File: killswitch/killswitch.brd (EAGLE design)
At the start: 42.3 x 42.3 mm, 28 parts, among them U1 CD74AC20M96, U2 MMBT2222ALT1G, U3 MMBT3906LT1G

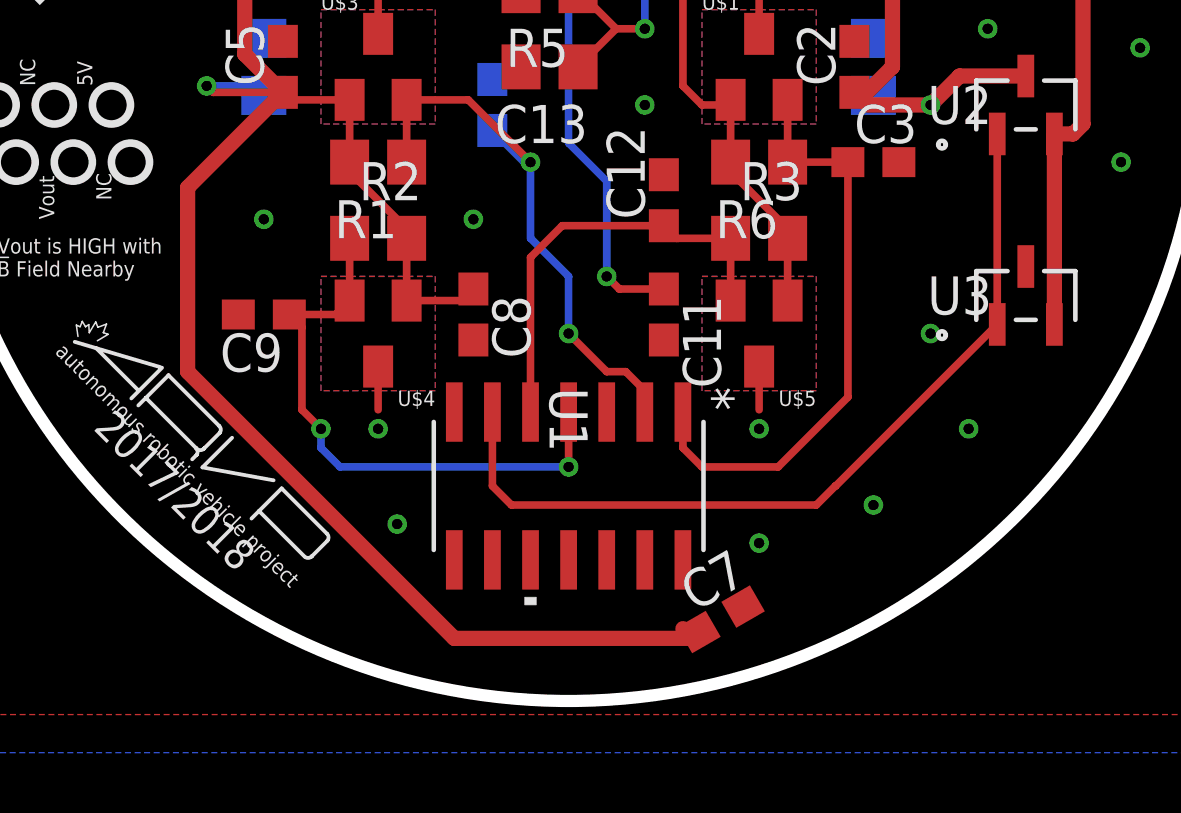
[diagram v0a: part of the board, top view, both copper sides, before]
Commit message: Miss spec'ed a part
NAND gate I choose only went up to 3.3V, I swapped it out with one
that'll go up to 5V.
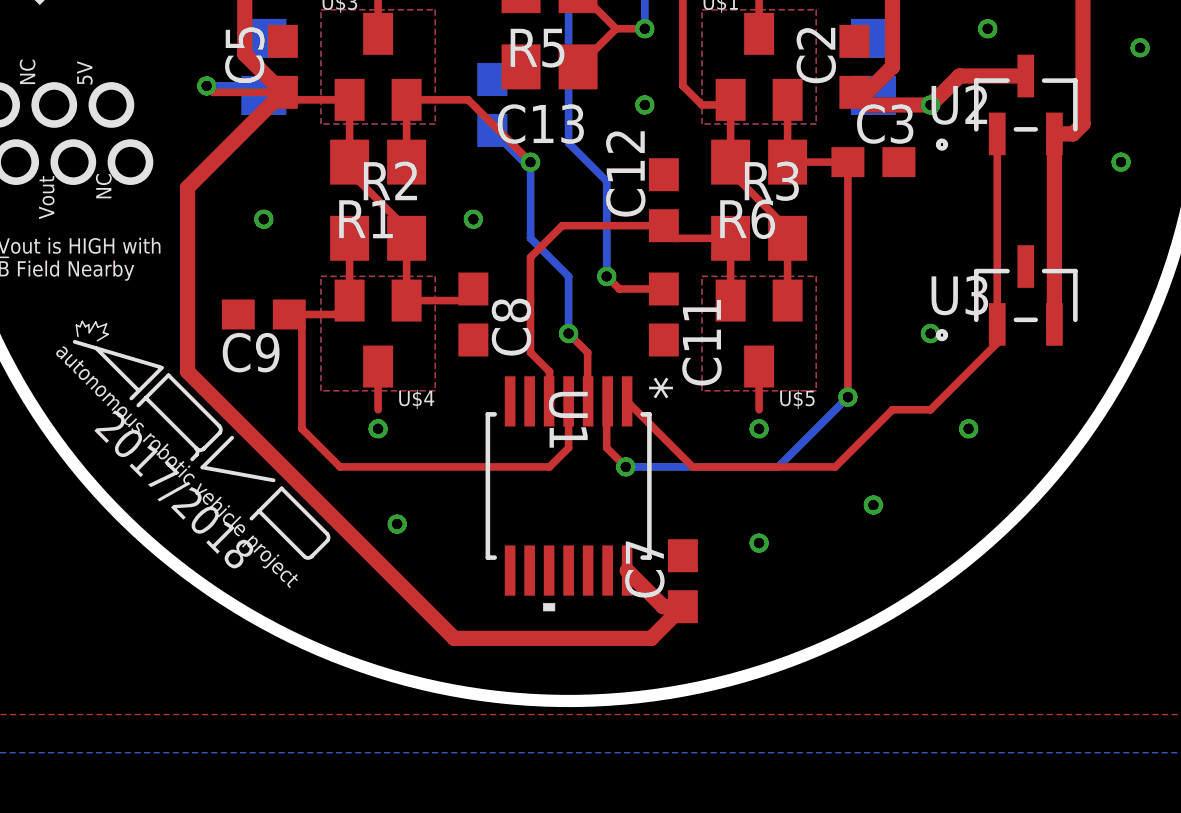
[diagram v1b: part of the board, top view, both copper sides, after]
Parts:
- U1: value CD74AC20M96 -> CD4012BPWR; device KillSwitch:D14 -> KillSwitch:PW14
- moved C7 1.80 mm to (24.1, 0.64), turned to 90 degrees
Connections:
- net GND: now also U1.6, U1.8; no longer U1.13
- net N$1: now also U1.3; no longer U1.2
- net N$5: now also U1.2; no longer U1.1
- net N$6: now also U1.1; no longer U1.6
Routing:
- net N$6: track 28.4 -> 21.9 mm
- net N$5: track 19.8 -> 22.7 mm, vias 0 -> 2
- net +5V: track 145.7 -> 147.4 mm
- net N$1: track 18.3 -> 17.5 mm
- net N$2: vias 2 -> 0
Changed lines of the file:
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@@
 <element name="R5" library="resistor" library_urn="urn:adsk.eagle:library:348" package="R0805" package3d_urn="urn:adsk.eagle:package:26059/1" value="10k" x="19.685" y="20.32" rot="R180"/>
 <element name="C13" library="resistor" library_urn="urn:adsk.eagle:library:348" package="C0805" package3d_urn="urn:adsk.eagle:package:26137/1" value="2.2uF" x="19.685" y="17.78" rot="R180"/>
-<element name="C7" library="resistor" library_urn="urn:adsk.eagle:library:348" package="C0603" package3d_urn="urn:adsk.eagle:package:26138/1" value="1uF" x="25.4" y="-0.635" rot="R30"/>
+<element name="C7" library="resistor" library_urn="urn:adsk.eagle:library:348" package="C0603" package3d_urn="urn:adsk.eagle:package:26138/1" value="1uF" x="24.13" y="0.635" rot="R90"/>
 <element name="R4" library="resistor" library_urn="urn:adsk.eagle:library:348" package="R0805" package3d_urn="urn:adsk.eagle:package:26059/1" value="320" x="34.29" y="27.305" rot="R135"/>
 <element name="LED1" library="SparkFun (2015_10_14 22_27_04 UTC)" package="LED-1206" value="" x="30.48" y="31.115" rot="R135"/>
-<element name="U1" library="KillSwitch" library_urn="urn:adsk.eagle:library:576207" package="D14" value="CD74AC20M96" x="20.32" y="3.81" rot="R270">
-<attribute name="MANUFACTURER_PART_NUMBER" value="CD74AC20M96" x="20.32" y="3.81" size="1.778" layer="27" rot="R270" display="off"/>
-<attribute name="VENDOR" value="Texas Instruments" x="20.32" y="3.81" size="1.778" layer="27" rot="R270" display="off"/>
+<element name="U1" library="KillSwitch" library_urn="urn:adsk.eagle:library:576207" package="PW14" value="CD4012BPWR" x="20.32" y="3.81" rot="R270">
+<attribute name="MANUFACTURER_PART_NUMBER" value="CD4012BPWR" x="20.32" y="3.81" size="1.778" layer="27" rot="R270" display="off"/>
+<attribute name="VENDOR" value="Vendor" x="20.32" y="3.81" size="1.778" layer="27" rot="R270" display="off"/>
 </element>
 </elements>
@@
 <via x="24.765" y="29.845" extent="1-16" drill="0.35"/>
 <contactref element="U1" pad="7"/>
-<contactref element="U1" pad="13"/>
+<contactref element="U1" pad="6"/>
 <contactref element="U1" pad="12"/>
 <contactref element="U1" pad="11"/>
 <contactref element="U1" pad="10"/>
 <contactref element="U1" pad="9"/>
+<contactref element="U1" pad="8"/>
 </signal>
 <signal name="+5V">
@@
 <wire x1="31.115" y1="17.78" x2="30.055" y2="16.72" width="0.508" layer="1"/>
 <contactref element="C7" pad="1"/>
-<wire x1="7.62" y1="7.62" x2="16.51" y2="-1.27" width="0.508" layer="1"/>
-<wire x1="7.62" y1="7.62" x2="7.62" y2="13.755" width="0.508" layer="1"/>
+<wire x1="7.62" y1="13.755" x2="7.62" y2="7.62" width="0.508" layer="1"/>
 <wire x1="7.62" y1="13.755" x2="10.795" y2="16.93" width="0.508" layer="1"/>
 <wire x1="14.92" y1="9.99" x2="16.76" y2="9.99" width="0.254" layer="1"/>
@@
 <wire x1="22.86" y1="27.305" x2="22.225" y2="26.67" width="0.254" layer="1"/>
 <wire x1="31.115" y1="23.495" x2="27.305" y2="27.305" width="0.508" layer="1"/>
-<wire x1="24.453878125" y1="-1.27" x2="16.51" y2="-1.27" width="0.508" layer="1"/>
-<wire x1="24.453878125" y1="-1.27" x2="24.663878125" y2="-1.06" width="0.508" layer="1"/>
-<wire x1="24.13" y1="-0.946121875" x2="24.453878125" y2="-1.27" width="0.508" layer="1"/>
 <contactref element="U1" pad="14"/>
-<wire x1="24.13" y1="-0.946121875" x2="24.13" y2="1.3462" width="0" layer="19" extent="1-1"/>
+<wire x1="7.62" y1="7.62" x2="16.51" y2="-1.27" width="0.508" layer="1"/>
+<wire x1="16.51" y1="-1.27" x2="23.075" y2="-1.27" width="0.508" layer="1"/>
+<wire x1="23.075" y1="-1.27" x2="24.13" y2="-0.215" width="0.508" layer="1"/>
+<wire x1="24.13" y1="-0.215" x2="23.4756" y2="-0.215" width="0.508" layer="1"/>
+<wire x1="23.4756" y1="-0.215" x2="22.27" y2="0.9906" width="0.508" layer="1"/>
 </signal>
 <signal name="N$5">
@@
 <wire x1="27.62" y1="16.68" x2="27.62" y2="14.605" width="0.254" layer="1"/>
 <wire x1="27.62" y1="14.605" x2="29.63" y2="14.605" width="0.254" layer="1"/>
-<contactref element="U1" pad="1"/>
 <wire x1="29.63" y1="14.605" x2="29.63" y2="6.77" width="0.254" layer="1"/>
-<wire x1="29.63" y1="6.77" x2="27.305" y2="4.445" width="0.254" layer="1"/>
-<wire x1="24.765" y1="4.445" x2="24.13" y2="5.08" width="0.254" layer="1"/>
-<wire x1="24.13" y1="5.08" x2="24.13" y2="6.2738" width="0.254" layer="1"/>
-<wire x1="27.305" y1="4.445" x2="24.765" y2="4.445" width="0.254" layer="1"/>
+<contactref element="U1" pad="2"/>
+<via x="29.63" y="6.77" extent="1-16" drill="0.35"/>
+<wire x1="29.63" y1="6.77" x2="27.305" y2="4.445" width="0.254" layer="16"/>
+<wire x1="27.305" y1="4.445" x2="22.225" y2="4.445" width="0.254" layer="16"/>
+<via x="22.225" y="4.445" extent="1-16" drill="0.35"/>
+<wire x1="22.225" y1="4.445" x2="21.59" y2="5.08" width="0.254" layer="1"/>
+<wire x1="21.59" y1="5.08" x2="21.59" y2="6.5994" width="0.254" layer="1"/>
+<wire x1="21.59" y1="6.5994" x2="21.62" y2="6.6294" width="0.254" layer="1"/>
 </signal>
 <signal name="N$1">
@@
 <wire x1="20.32" y1="10.795" x2="20.32" y2="8.89" width="0.254" layer="16"/>
 <via x="20.32" y="8.89" extent="1-16" drill="0.35"/>
-<wire x1="20.32" y1="8.89" x2="21.59" y2="7.62" width="0.254" layer="1"/>
 <wire x1="19.05" y1="14.605" x2="19.05" y2="12.065" width="0.254" layer="16"/>
 <wire x1="14.92" y1="16.68" x2="14.92" y2="14.605" width="0.254" layer="1"/>
-<contactref element="U1" pad="2"/>
-<wire x1="21.59" y1="7.62" x2="22.225" y2="7.62" width="0.254" layer="1"/>
-<wire x1="22.225" y1="7.62" x2="22.86" y2="6.985" width="0.254" layer="1"/>
-<wire x1="22.86" y1="6.985" x2="22.86" y2="6.2738" width="0" layer="19" extent="1-1"/>
+<contactref element="U1" pad="3"/>
+<wire x1="20.32" y1="8.89" x2="20.955" y2="8.255" width="0.254" layer="1"/>
+<wire x1="20.955" y1="8.255" x2="20.955" y2="6.6444" width="0.254" layer="1"/>
+<wire x1="20.955" y1="6.6444" x2="20.97" y2="6.6294" width="0.254" layer="1"/>
 </signal>
 <signal name="N$2">
@@
 <wire x1="11.01" y1="9.525" x2="11.43" y2="9.105" width="0.254" layer="1"/>
 <contactref element="U1" pad="4"/>
-<wire x1="11.43" y1="6.35" x2="12.065" y2="5.715" width="0.254" layer="1"/>
-<via x="12.065" y="5.715" extent="1-16" drill="0.35"/>
-<wire x1="12.065" y1="5.715" x2="12.065" y2="5.08" width="0.254" layer="16"/>
-<wire x1="12.065" y1="5.08" x2="12.7" y2="4.445" width="0.254" layer="16"/>
-<wire x1="12.7" y1="4.445" x2="20.32" y2="4.445" width="0.254" layer="16"/>
-<via x="20.32" y="4.445" extent="1-16" drill="0.35"/>
-<wire x1="20.32" y1="4.445" x2="20.32" y2="6.2738" width="0.254" layer="1"/>
-<wire x1="11.43" y1="9.105" x2="11.43" y2="6.35" width="0.254" layer="1"/>
+<wire x1="11.43" y1="9.105" x2="11.43" y2="5.715" width="0.254" layer="1"/>
+<wire x1="11.43" y1="5.715" x2="12.7" y2="4.445" width="0.254" layer="1"/>
+<wire x1="19.685" y1="4.445" x2="20.32" y2="5.08" width="0.254" layer="1"/>
+<wire x1="20.32" y1="5.08" x2="20.32" y2="6.6294" width="0.254" layer="1"/>
+<wire x1="12.7" y1="4.445" x2="19.685" y2="4.445" width="0.254" layer="1"/>
 </signal>
 <signal name="N$3">
@@
 <wire x1="25.72" y1="12.065" x2="25.72" y2="9.99" width="0.254" layer="1"/>
 <contactref element="U1" pad="5"/>
-<wire x1="19.05" y1="11.43" x2="19.05" y2="6.2738" width="0.254" layer="1"/>
+<wire x1="19.05" y1="11.43" x2="19.05" y2="8.255" width="0.254" layer="1"/>
+<wire x1="19.05" y1="8.255" x2="19.685" y2="7.62" width="0.254" layer="1"/>
+<wire x1="19.685" y1="7.62" x2="19.685" y2="6.6444" width="0.254" layer="1"/>
+<wire x1="19.685" y1="6.6444" x2="19.67" y2="6.6294" width="0.254" layer="1"/>
 </signal>
 <signal name="N$6">
 <contactref element="U3" pad="1"/>
 <contactref element="U2" pad="1"/>
-<wire x1="34.6075" y1="9.1948" x2="29.2227" y2="3.81" width="0.254" layer="1"/>
 <wire x1="34.6075" y1="15.5448" x2="34.6075" y2="9.1948" width="0.254" layer="1"/>
-<contactref element="U1" pad="6"/>
-<wire x1="29.2227" y1="3.81" x2="29.21" y2="3.81" width="0.254" layer="1"/>
-<wire x1="29.21" y1="3.81" x2="28.575" y2="3.175" width="0.254" layer="1"/>
-<wire x1="28.575" y1="3.175" x2="18.415" y2="3.175" width="0.254" layer="1"/>
-<wire x1="18.415" y1="3.175" x2="17.78" y2="3.81" width="0.254" layer="1"/>
-<wire x1="17.78" y1="3.81" x2="17.78" y2="6.2738" width="0.254" layer="1"/>
+<contactref element="U1" pad="1"/>
+<wire x1="34.6075" y1="9.1948" x2="34.6075" y2="8.5725" width="0.254" layer="1"/>
+<wire x1="34.6075" y1="8.5725" x2="32.385" y2="6.35" width="0.254" layer="1"/>
+<wire x1="32.385" y1="6.35" x2="31.115" y2="6.35" width="0.254" layer="1"/>
+<wire x1="29.21" y1="4.445" x2="24.4544" y2="4.445" width="0.254" layer="1"/>
+<wire x1="24.4544" y1="4.445" x2="22.27" y2="6.6294" width="0.254" layer="1"/>
+<wire x1="31.115" y1="6.35" x2="29.21" y2="4.445" width="0.254" layer="1"/>
 </signal>
 <signal name="OUTPUT">

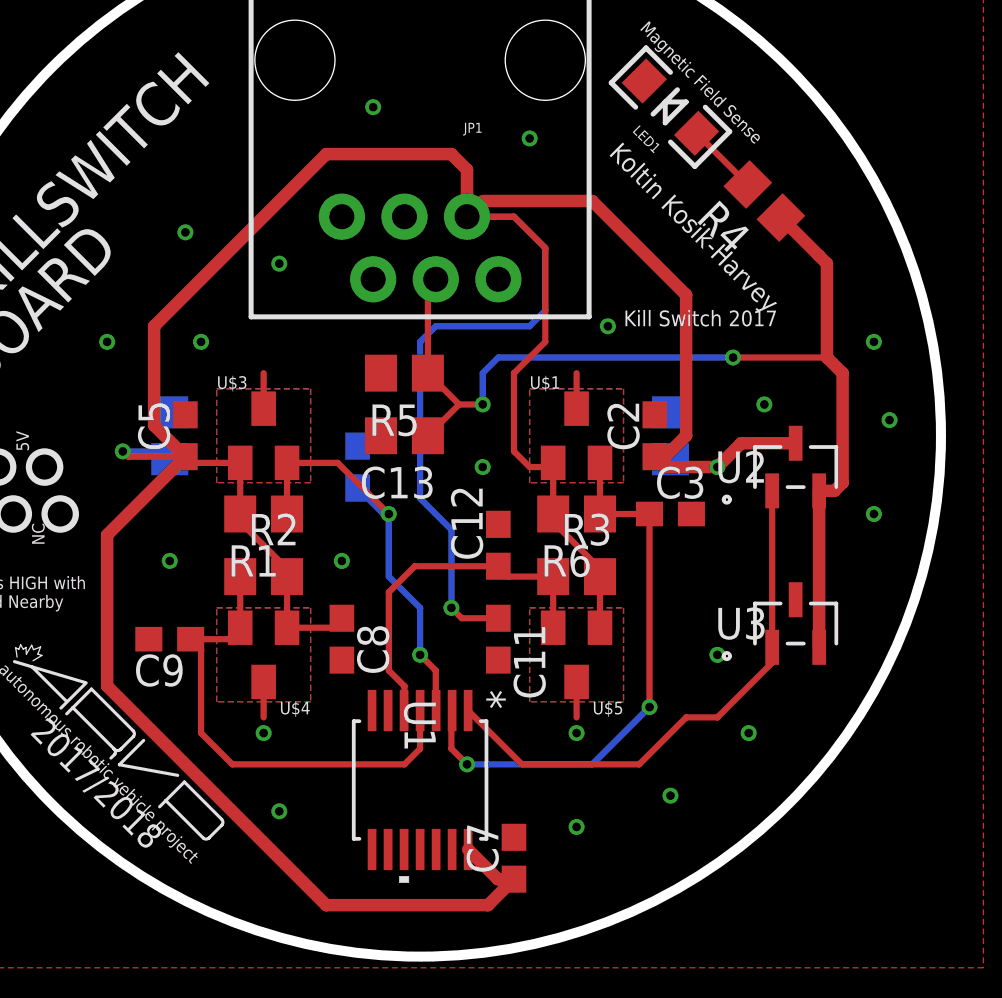
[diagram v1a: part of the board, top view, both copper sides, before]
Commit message: Using MOS output buffer
-also added EAGLE libraries
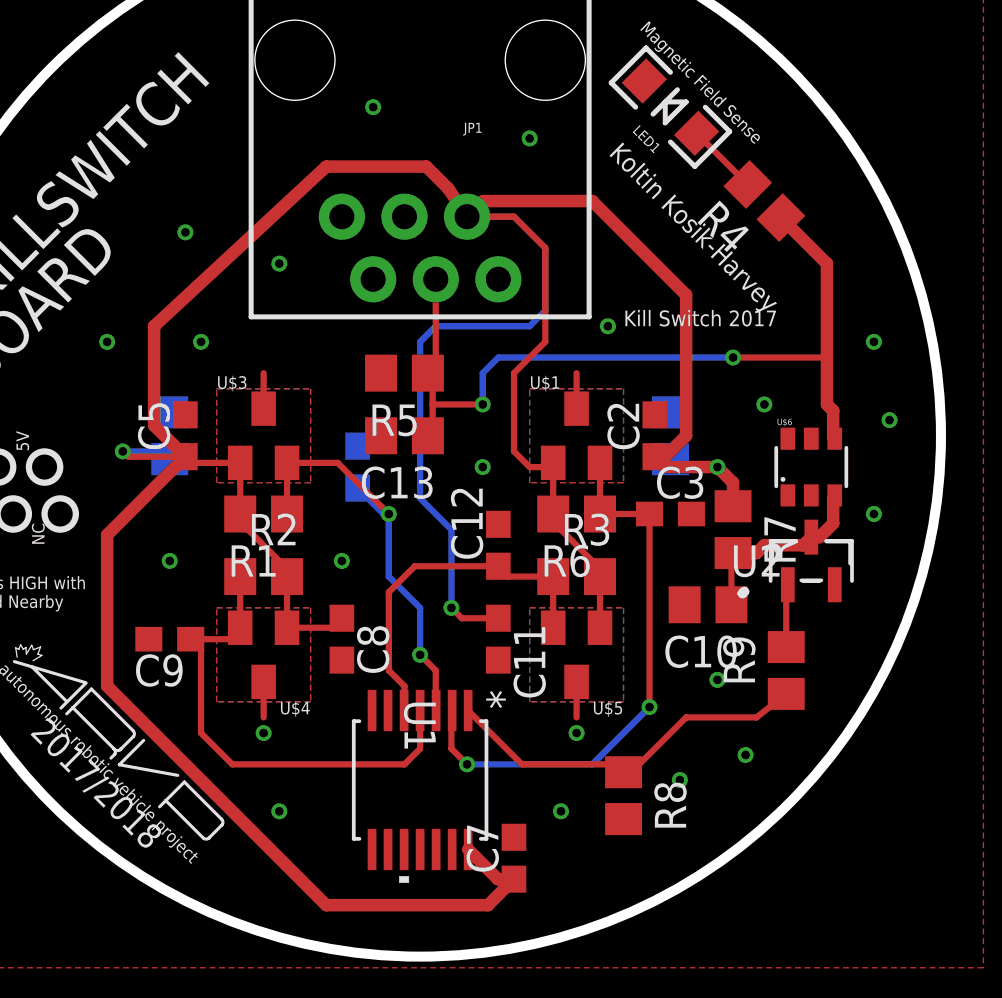
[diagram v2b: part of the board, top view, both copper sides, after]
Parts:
- removed U3: MMBT3906LT1G, KillSwitch:SOT-23
- added C10: 100nF, resistor:C0805
- added R7, R8: 10k, resistor:R0805
- added R9: 1k, resistor:R0805
- added U$6: DMP2066LDM-7, KillSwitch:SOT23-6
- U2: value MMBT2222ALT1G -> 2N7002-7-F
- moved U2 3.86 mm to (36.2, 12.7)
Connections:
- removed net N$6: U1.1, U2.1, U3.1
- new net N$10: R9.2, U2.1
- new net N$9: C10.1, R7.2, U$6.GATE, U2.3
- new net NAND_OUTPUT: R8.1, R9.1, U1.1
- net +5V: now also R7.1; no longer U2.3
- net GND: now also C10.2, R8.2, U2.2; no longer U3.3
- net OUTPUT: now also U$6.SOURCE; no longer U2.2, U3.2
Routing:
- net N$6: track 21.9 -> 0.00 mm
- net NAND_OUTPUT: track 0.00 -> 15.7 mm
- net OUTPUT: track 43.2 -> 34.5 mm
- net N$9: track 0.00 -> 7.85 mm
- net +5V: track 147.4 -> 144.1 mm
- net N$10: track 0.00 -> 2.54 mm
